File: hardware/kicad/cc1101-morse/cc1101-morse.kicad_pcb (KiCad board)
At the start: 2 copper layers, 40 x 60 mm, 14 parts, among them J1 Conn_02x04_Odd_Even, J2 Conn_01x02_Socket, J3 Conn_01x02_Socket, SW1 SW_Push, U1 ESP32-C3-SuperMini

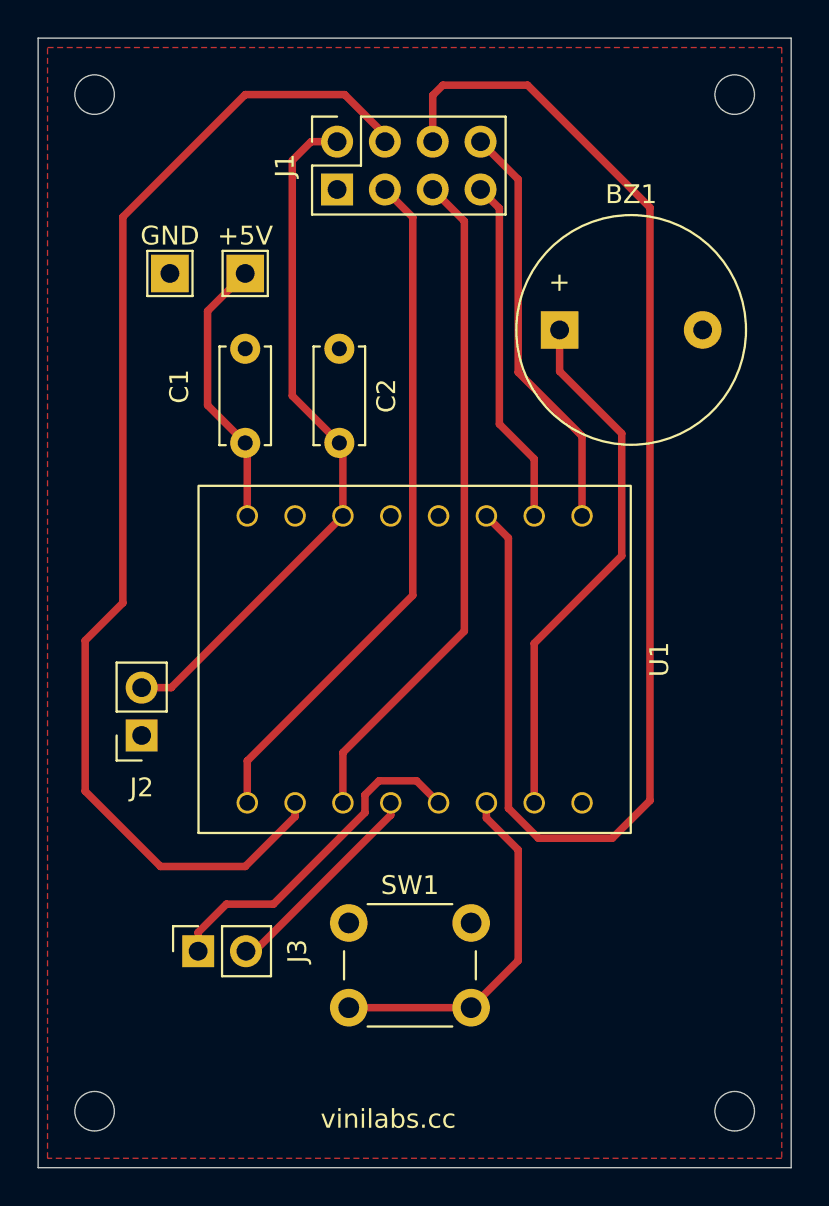
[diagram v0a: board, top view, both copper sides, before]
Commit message: Move all copper to the back for single-sided laminate
The stock has copper on one face and bare substrate on the other, so
copper on F.Cu described a board that was never going to be made.
Components sit on the bare face, leads pass through, and soldering
happens on the copper face — the standard single-sided through-hole
build.

69 track segments and the ground pour moved to B.Cu. Nothing else
changed: through-hole pads are defined on *.Cu and already existed on
both layers, so the routing is identical, just on the other side.

DRC clean: 0 unconnected, 0 parity. The one violation is the expected
footprint/library mismatch from the earlier pad renumbering.

What this adds is a new way to ruin a board, so it is written down.
KiCad draws every layer from the top, which makes a B.Cu export a view
*through* the laminate — engrave it as exported and every footprint
lands mirrored. fabrication.md now carries the flip and a check that
catches it: the board is asymmetric, so J1 at the top edge and the
vinilabs.cc silkscreen tell you immediately if the mirroring is wrong.

Exports regenerated from B.Cu and committed. Hole count and parts
count corrected to 44 and 10 across the docs, and the README Status
section updated — it still claimed the radio was untested.
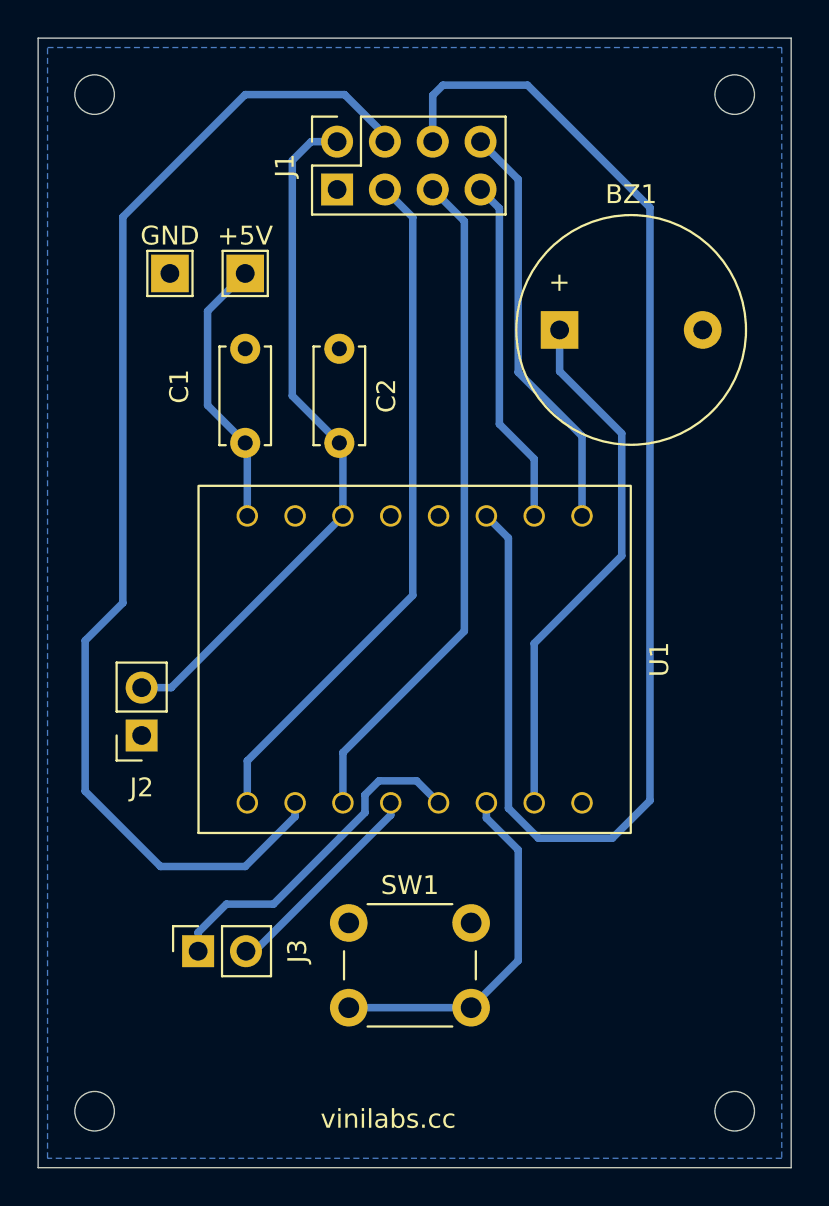
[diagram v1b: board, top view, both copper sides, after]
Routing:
- added copper zone on B.Cu, net GND
- removed copper zone on F.Cu, net GND

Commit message: Replace J2/J3 with one 4-pin display socket, plus a +3V3 wire link
J2 is now a single 1x4 female socket — GND, +3V3, GPIO9 (SCL),
GPIO8 (SDA) — so an SSD1306 plugs straight in instead of spanning two
separate 2-pin headers. J3 is gone.

+3V3 cannot reach it in copper. J1 pin 4 and its trace sit directly
between the rail and the connector, and on one layer a trace cannot
cross a trace. TP3 and TP4 are pads for a soldered wire link, which
§3 otherwise forbids, so §14 records why this one is allowed.

The workaround that looks better is worse. The rail can be threaded
between U1 pads 9 and 10 — 1.70 mm of gap against the 1.20 mm a
0.4 mm trace needs, and DRC passes. But it leaves ~0.25 mm of pour
either side, and that pour is the ground return for J1 pin 1, the
CC1101's ground. The trade is a visible wire against a severed RF
ground plane: one costs ten seconds of soldering, the other is
invisible, passes every check, and surfaces later as poor range.

DRC will report +3V3 unconnected. That is correct — the net arrives
in two pieces and the link is off-board. Two courtyard overlaps on
TP4/U1 are also expected: the ESP32 sits on female headers, so its
body clears a pad underneath.

Exports regenerated. 46 holes now, 11 parts to solder; counts updated
across the docs.
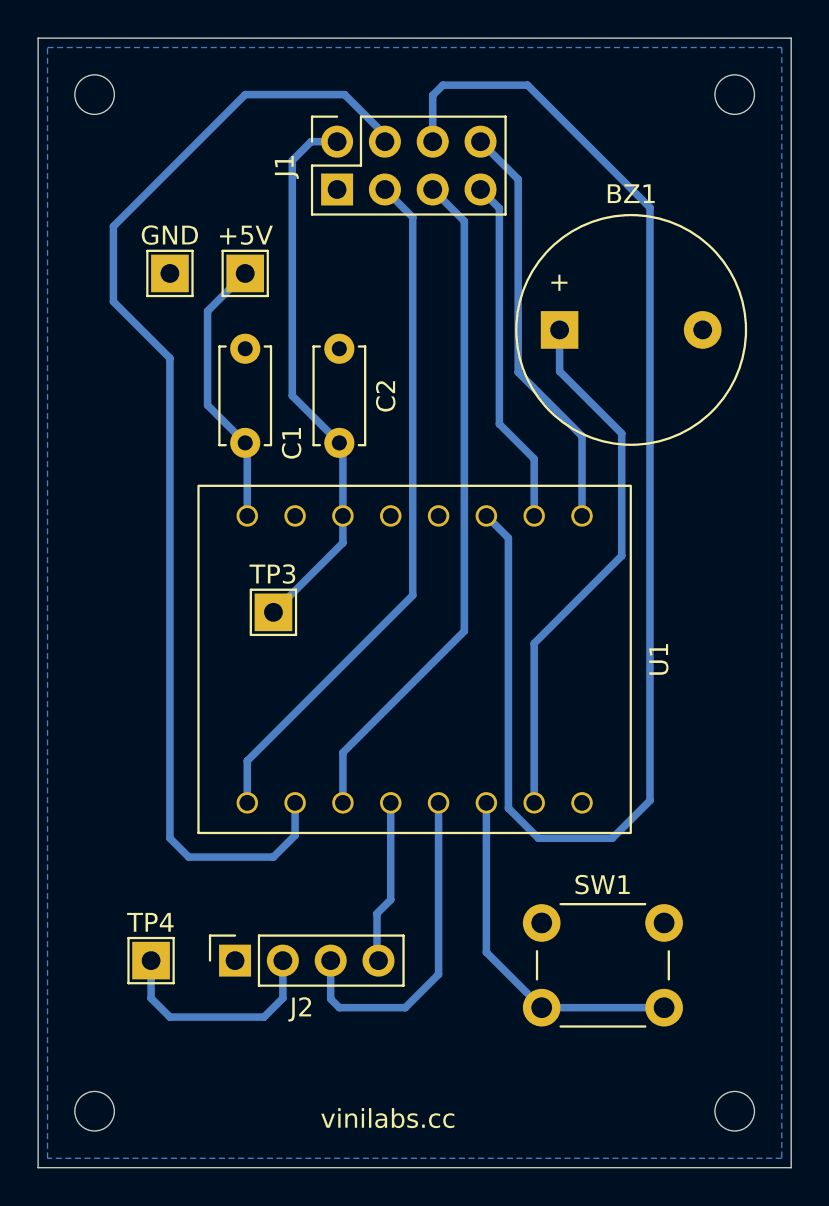
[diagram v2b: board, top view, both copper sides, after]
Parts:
- removed J3: Conn_01x02_Socket, Connector_PinSocket_2.54mm:PinSocket_1x02_P2.54mm_Vertical
- added TP3: TestPoint, TestPoint:TestPoint_THTPad_2.0x2.0mm_Drill1.0mm, F.Cu at (142.5, 101.0)
- added TP4: TestPoint, TestPoint:TestPoint_THTPad_2.0x2.0mm_Drill1.0mm, F.Cu at (136.0, 119.5)
- J2: value Conn_01x02_Socket -> Conn_01x04_Socket; footprint Connector_PinSocket_2.54mm:PinSocket_1x02_P2.54mm_Vertical -> Connector_PinSocket_2.54mm:PinSocket_1x04_P2.54mm_Vertical
- moved J2 12.9 mm to (140.5, 119.5), turned to 90 degrees
- moved SW1 10.2 mm to (156.8, 117.5)
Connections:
- U1 pad 12: Net-(J3-Pin_2) -> Net-(J2-Pin_4)
- U1 pad 13: Net-(J3-Pin_1) -> Net-(J2-Pin_3)
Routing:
- net Net-(J3-Pin_1): track 18.1 -> 0.00 mm
- net Net-(J2-Pin_3): track 0.00 -> 17.8 mm
- net Net-(J3-Pin_2): track 11.3 -> 0.00 mm
- net Net-(J2-Pin_4): track 0.00 -> 8.72 mm
- net +3V3: track 37.0 -> 41.3 mm
- net Net-(J1-Pin_4): track 63.8 -> 61.6 mm
- net Net-(U1-GPIO10): track 19.1 -> 18.6 mm

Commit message: Fixing routes
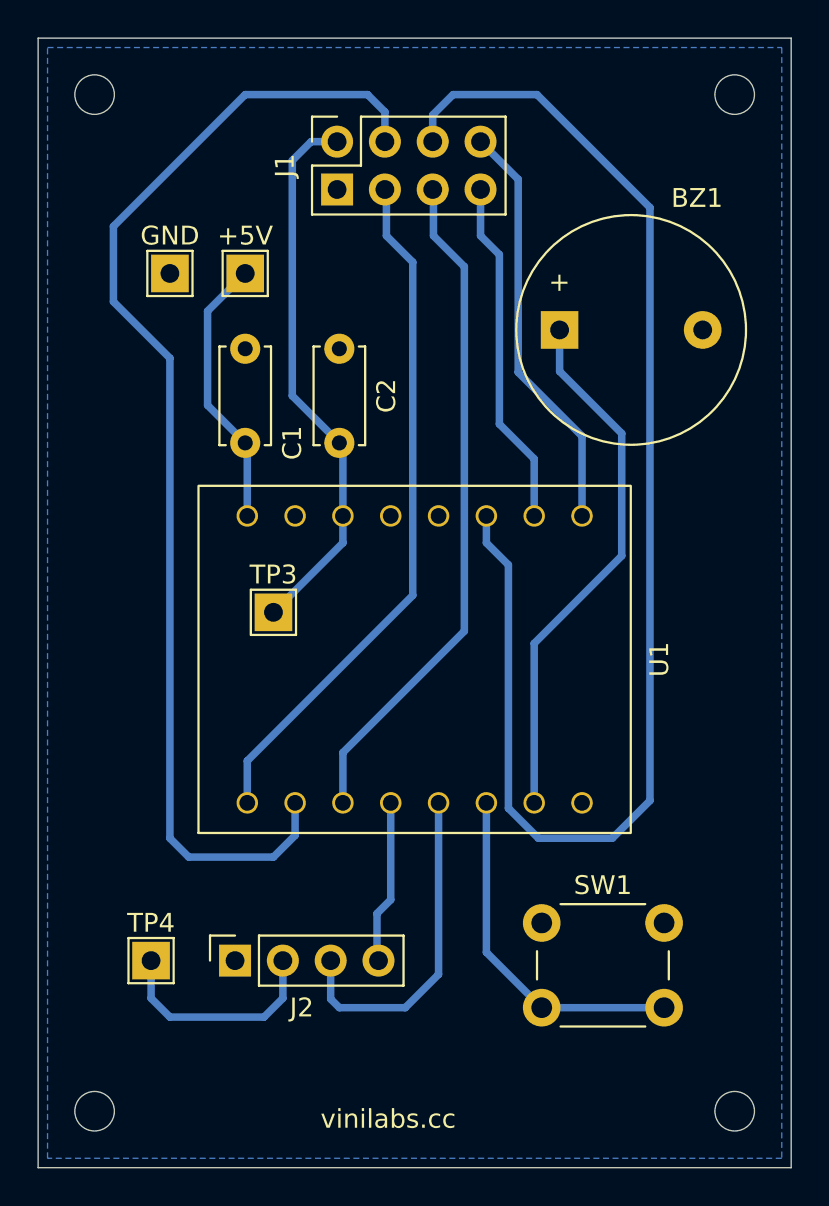
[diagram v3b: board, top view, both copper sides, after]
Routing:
- net Net-(J1-Pin_6): track 73.4 -> 72.4 mm
- net Net-(J1-Pin_4): track 61.6 -> 62.3 mm
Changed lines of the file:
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@@
 		(tags "buzzer")
 		(property "Reference" "BZ1"
-			(at 3.8 -7.2 0)
+			(at 7.3 -7 0)
 			(layer "F.SilkS")
 			(effects
@@
 	)
 	(segment
+		(start 155.5 78)
+		(end 155.5 88.249758)
+		(width 0.4)
+		(layer "B.Cu")
+		(net "Net-(J1-Pin_8)")
+	)
+	(segment
 		(start 155.5 88.249758)
 		(end 158.89 91.639758)
@@
 	)
 	(segment
-		(start 155.5 78)
-		(end 155.5 88.249758)
+		(start 153.5 81)
+		(end 154.5 82)
 		(width 0.4)
 		(layer "B.Cu")
-		(net "Net-(J1-Pin_8)")
+		(net "Net-(J1-Pin_7)")
 	)
 	(segment
-		(start 153.5 78.54)
-		(end 154.5 79.54)
+		(start 154.5 82)
+		(end 154.5 91)
 		(width 0.4)
 		(layer "B.Cu")
@@
 	)
 	(segment
-		(start 154.5 79.54)
-		(end 154.5 91)
+		(start 156.35 92.85)
+		(end 156.35 95.88)
 		(width 0.4)
 		(layer "B.Cu")
@@
 	)
 	(segment
-		(start 156.35 92.85)
-		(end 156.35 95.88)
+		(start 153.5 78.54)
+		(end 153.5 81)
 		(width 0.4)
 		(layer "B.Cu")
@@
 	)
 	(segment
-		(start 150.96 76)
-		(end 150.96 73.54)
+		(start 162.5 111)
+		(end 160.5 113)
 		(width 0.4)
 		(layer "B.Cu")
@@
 	)
 	(segment
-		(start 154.98 111.40463)
-		(end 154.98 97.05)
+		(start 162.5 79.5)
+		(end 162.5 111)
 		(width 0.4)
 		(layer "B.Cu")
@@
 	)
 	(segment
-		(start 156 73)
-		(end 162.5 79.5)
+		(start 150.96 74.58)
+		(end 152.04 73.5)
+		(width 0.4)
+		(layer "B.Cu")
+		(net "Net-(J1-Pin_6)")
+	)
+	(segment
+		(start 153.81 97.31)
+		(end 153.81 95.88)
 		(width 0.4)
 		(layer "B.Cu")
@@
 	)
 	(segment
-		(start 151.5 73)
-		(end 156 73)
+		(start 154.98 98.48)
+		(end 153.81 97.31)
 		(width 0.4)
 		(layer "B.Cu")
@@
 	)
 	(segment
-		(start 162.5 79.5)
-		(end 162.5 111)
+		(start 156.57537 113)
+		(end 154.98 111.40463)
 		(width 0.4)
 		(layer "B.Cu")
@@
 	)
 	(segment
-		(start 150.96 73.54)
-		(end 151.5 73)
+		(start 154.98 111.40463)
+		(end 154.98 98.48)
 		(width 0.4)
 		(layer "B.Cu")
@@
 	)
 	(segment
-		(start 162.5 111)
-		(end 160.5 113)
+		(start 156.5 73.5)
+		(end 162.5 79.5)
 		(width 0.4)
 		(layer "B.Cu")
@@
 	)
 	(segment
-		(start 154.98 97.05)
-		(end 153.81 95.88)
+		(start 152.04 73.5)
+		(end 156.5 73.5)
 		(width 0.4)
 		(layer "B.Cu")
@@
 	)
 	(segment
-		(start 156.57537 113)
-		(end 154.98 111.40463)
+		(start 150.96 76)
+		(end 150.96 74.58)
 		(width 0.4)
 		(layer "B.Cu")
@@
 	)
 	(segment
-		(start 149.9 100.1)
-		(end 149.9 80.02)
+		(start 148.5 81)
+		(end 148.5 78.62)
 		(width 0.4)
 		(layer "B.Cu")
@@
 	)
 	(segment
-		(start 149.9 80.02)
+		(start 148.5 78.62)
 		(end 148.42 78.54)
 		(width 0.4)
@@
 	)
 	(segment
-		(start 143.65 112.85)
-		(end 143.65 111.12)
+		(start 149.9 100.1)
+		(end 149.9 82.4)
+		(width 0.4)
+		(layer "B.Cu")
+		(net "Net-(J1-Pin_3)")
+	)
+	(segment
+		(start 149.9 82.4)
+		(end 148.5 81)
+		(width 0.4)
+		(layer "B.Cu")
+		(net "Net-(J1-Pin_3)")
+	)
+	(segment
+		(start 148.42 74.42)
+		(end 147.5 73.5)
 		(width 0.4)
 		(layer "B.Cu")
@@
 	)
 	(segment
-		(start 146.28 73.5)
-		(end 141 73.5)
+		(start 137 87.5)
+		(end 137 113)
 		(width 0.4)
 		(layer "B.Cu")
@@
 	)
 	(segment
-		(start 137 113)
-		(end 138 114)
+		(start 138 114)
+		(end 142.5 114)
 		(width 0.4)
 		(layer "B.Cu")
@@
 	)
 	(segment
-		(start 148.42 76)
-		(end 148.42 75.64)
+		(start 137 113)
+		(end 138 114)
 		(width 0.4)
 		(layer "B.Cu")
@@
 	)
 	(segment
-		(start 148.42 75.64)
-		(end 146.28 73.5)
+		(start 147.5 73.5)
+		(end 141 73.5)
 		(width 0.4)
 		(layer "B.Cu")
@@
 	)
 	(segment
+		(start 148.42 76)
+		(end 148.42 74.42)
+		(width 0.4)
+		(layer "B.Cu")
+		(net "Net-(J1-Pin_4)")
+	)
+	(segment
 		(start 141 73.5)
 		(end 134 80.5)
@@
 	)
 	(segment
+		(start 143.65 112.85)
+		(end 143.65 111.12)
+		(width 0.4)
+		(layer "B.Cu")
+		(net "Net-(J1-Pin_4)")
+	)
+	(segment
 		(start 134 84.5)
 		(end 137 87.5)
@@
 	)
 	(segment
-		(start 137 87.5)
-		(end 137 113)
+		(start 152.64 102)
+		(end 146.19 108.45)
 		(width 0.4)
 		(layer "B.Cu")
-		(net "Net-(J1-Pin_4)")
+		(net "Net-(J1-Pin_5)")
 	)
 	(segment
-		(start 138 114)
-		(end 142.5 114)
+		(start 146.19 108.45)
+		(end 146.19 111.12)
 		(width 0.4)
 		(layer "B.Cu")
-		(net "Net-(J1-Pin_4)")
+		(net "Net-(J1-Pin_5)")
 	)
 	(segment
-		(start 150.96 78.54)
-		(end 152.64 80.22)
+		(start 152.64 82.64)
+		(end 152.64 102)
 		(width 0.4)
 		(layer "B.Cu")
@@
 	)
 	(segment
-		(start 146.19 111.12)
-		(end 146.19 108.45)
+		(start 151 78.58)
+		(end 151 81)
 		(width 0.4)
 		(layer "B.Cu")
@@
 	)
 	(segment
-		(start 146.19 108.45)
-		(end 152.64 102)
+		(start 150.96 78.54)
+		(end 151 78.58)
 		(width 0.4)
 		(layer "B.Cu")
@@
 	)
 	(segment
-		(start 152.64 80.22)
-		(end 152.64 102)
+		(start 151 81)
+		(end 152.64 82.64)
 		(width 0.4)
 		(layer "B.Cu")
